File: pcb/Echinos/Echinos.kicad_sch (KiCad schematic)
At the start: 26 parts, among them J1 USB_C_Receptacle_USB2.0, J2 TagConnect_6pins, J3 Pogo, J4 Conn_01x12_Socket, SW1 SW_Push, SW2 SW_Push, U2 W25Q128JVS, U4 USBLC6-2P6, U5 XC6210B332MR-G

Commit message: ✨ ♻️ 🚧 [PCB] - Continue draft schematic with:   - Keyboard matrix + Rotary encoder + analog joystick (specific sheet)   - Rename RP2040 sheet from untitled to RP2040 (make more sense ...)   - MCU first pin assignation
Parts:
- removed C13: 100n, Capacitor_SMD:C_0402_1005Metric, symbol Device:C
- removed C14, C18, C19: 1µ, Capacitor_SMD:C_0603_1608Metric, symbol Device:C
- removed D1: LED, symbol Device:LED
- removed D2: B5817, Diode_SMD:D_SOD-323, symbol Device:D_Schottky
- removed F1: 500mA, Fuse:Fuse_0603_1608Metric, symbol Device:Polyfuse
- removed FB1: FerriteBead_Small, symbol Device:FerriteBead_Small
- removed J1: USB_C_Receptacle_USB2.0, symbol Connector:USB_C_Receptacle_USB2.0
- removed J2: TagConnect_6pins, Connector:Tag-Connect_TC2030-IDC-FP_2x03_P1.27mm_Vertical, symbol Connector:Conn_ARM_SWD_TagConnect_TC2030
- removed J3: Pogo, ptechinos:Pogo_1x04_P2.5mm, symbol Connector_Generic:Conn_01x04
- removed J4: Conn_01x12_Socket, Connector_FFC-FPC:Hirose_FH12-12S-0.5SH_1x12-1MP_P0.50mm_Horizontal, symbol Connector:Conn_01x12_Socket
- removed R10, R11: 4.7kΩ, ptechinos:R_0805_2012Metric, symbol Device:R_Small
- removed R12, R5: 1k, Resistor_SMD:R_0402_1005Metric, symbol Device:R
- removed R2, R3: 5.1k, Resistor_SMD:R_0402_1005Metric, symbol Device:R
- removed R?: 10k, Resistor_SMD:R_0402_1005Metric, symbol Device:R
- removed R?: 27, Resistor_SMD:R_0402_1005Metric, symbol Device:R
- removed SW1, SW2: SW_Push, Button_Switch_SMD:SW_SPST_CK_KXT3, symbol Switch:SW_Push
- removed U2: W25Q128JVS, Package_SO:SOIC-8_5.23x5.23mm_P1.27mm, symbol Memory_Flash:W25Q128JVS
- removed U4: USBLC6-2P6, Package_TO_SOT_SMD:SOT-666, symbol Power_Protection:USBLC6-2P6
- removed U5: XC6210B332MR-G, Package_TO_SOT_SMD:SOT-23-5, symbol Regulator_Linear:XC6210B332MR
- renumbered R6 to R1
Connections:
- net HAND renamed hand
- no-connect marks 4 -> 0
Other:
- removed sheet RP2040
- added sheet Left Side (Left.kicad_sch)
- note removed: "1) Create an all-round contact point between the PCB and the metal housing --> EMI shield 2) Use a ferrite bead to protect against high frequency and force a unique path to ground 3) Avoid any connection (floating) to avoid canceling host shield protection"
- note removed: "??? I2C ???"
- note removed: "Access to Serial Wire Debug multi-drop bus --> Universal tag connector"
- note removed: "Boot / Reset buttons"
- note removed: "Connection between halves"
- note removed: "Debug (Optional)"
- note removed: "ESD protection"
- note removed: "Flash memory"
- note removed: "Max Current Output = 700mA Max Voltage Input = 6V"
- note removed: "On/Off indicator"
- note removed: "Overcurrent protection"
- note removed: "Pull-up resistor used while device is powering up for it to work correctly Resistor must be close to the flash chip"
- note removed: "QSPI lines should be wired as close as possible to MCU to maintain signal integrity"
- note removed: "RP2040"
- note removed: "Resistor must be close to the flash chip Switch pushed (low) --> USB Bootloader Switch released (pulled high) --> Firmware"
- note removed: "Trackball / Trackpad (SPI)"
- note removed: "USB-C connector"
- note removed: "VCC options - 3V and remove R1 to Trackpad PCB - 5V and remove R1/R7/R8 to Trackpad PCB R1 removed --> I2C connection R7/R8 removed --> Support for 5V power"
- note removed: "Voltage clamp"
- note removed: "Voltage regulation"
- moved on the sheet: R1

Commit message: ♻️ [PCB] - Add ferrite bead between shield and ground. Assign hand solder footprints whenever possible. Complete footprint assignation.
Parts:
- R1: footprint Resistor_SMD:R_0402_1005Metric -> Resistor_SMD:R_0402_1005Metric_Pad0.72x0.64mm_HandSolder
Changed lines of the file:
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@@
       (effects (font (size 1.27 1.27)))
     )
-    (property "Footprint" "Resistor_SMD:R_0402_1005Metric" (at 171.45 33.528 90)
+    (property "Footprint" "Resistor_SMD:R_0402_1005Metric_Pad0.72x0.64mm_HandSolder" (at 171.45 33.528 90)
       (effects (font (size 1.27 1.27)) hide)
     )

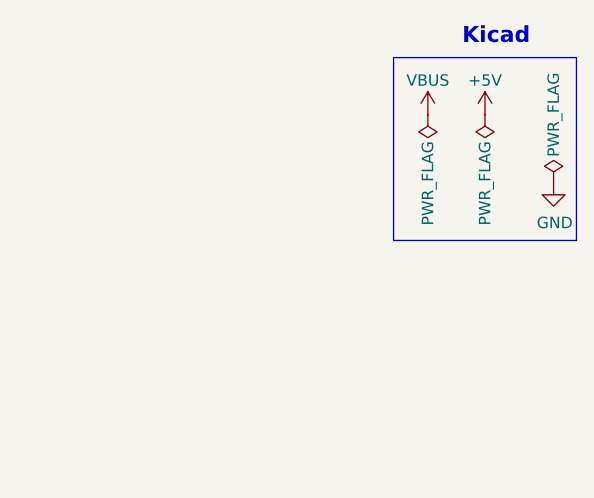
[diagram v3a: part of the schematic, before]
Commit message: ✨ 🐛 ✅ [PCB] - Pass ERC test (exception to unconnected GPIO pins). Fix power symbol assignation to please Kicad. Fix duplicated line name (encoder / joystick) to please Kicad. Add trackball sensor connection documentation. Assign newly created footprints (encoder, joystick, switch).
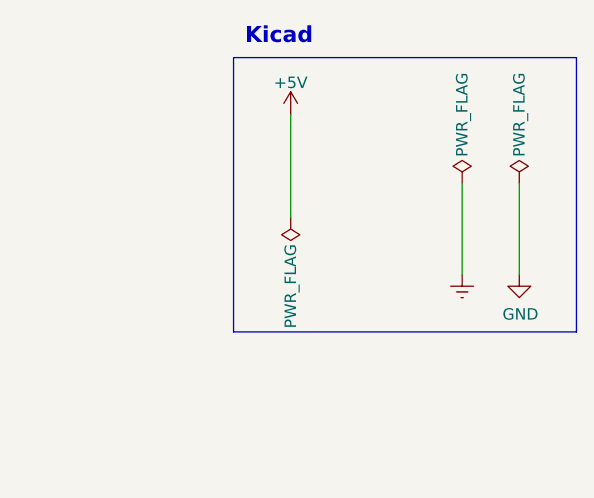
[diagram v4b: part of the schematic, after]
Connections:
- net +3V3 renamed +3.3V
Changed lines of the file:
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@@
     (date "2023-06-10")
   )
+  (wire (pts (xy 273.05 44.45) (xy 273.05 34.29))
+    (stroke (width 0) (type default))
+  )
   (wire (pts (xy 176.53 31.75) (xy 176.53 26.67))
     (stroke (width 0) (type default))
   )
+  (wire (pts (xy 266.7 44.45) (xy 266.7 34.29))
+    (stroke (width 0) (type default))
+  )
   (wire (pts (xy 163.83 31.75) (xy 167.64 31.75))
     (stroke (width 0) (type default))
   )
+  (wire (pts (xy 247.65 26.67) (xy 247.65 38.1))
+    (stroke (width 0) (type default))
+  )
   (wire (pts (xy 175.26 31.75) (xy 176.53 31.75))
     (stroke (width 0) (type default))
@@
     (fill (type none))
   )
-  (rectangle (start 259.08 20.32) (end 279.4 40.64)
+  (rectangle (start 241.3 20.32) (end 279.4 50.8)
     (stroke (width 0) (type default))
     (fill (type none))
@@
     (effects (font (size 1.778 1.778) (thickness 0.3556) bold) (justify left bottom))
   )
-  (text "Kicad" (at 266.7 19.05 0)
+  (text "Kicad" (at 242.57 19.05 0)
     (effects (font (size 1.778 1.778) (thickness 0.3556) bold) (justify left bottom))
   )
@@
     )
   )
-  (symbol (lib_id "power:VBUS") (at 262.89 26.67 0) (unit 1)
-    (in_bom yes) (on_board yes) (dnp no)
-    (property "Reference" "#PWR02" (at 262.89 30.48 0)
-      (effects (font (size 1.27 1.27)) hide)
-    )
-    (property "Value" "VBUS" (at 262.89 22.86 0)
-      (effects (font (size 1.27 1.27)))
-    )
-    (property "Footprint" "" (at 262.89 26.67 0)
-      (effects (font (size 1.27 1.27)) hide)
-    )
-    (property "Datasheet" "" (at 262.89 26.67 0)
+  (symbol (lib_id "power:+5V") (at 247.65 26.67 0) (unit 1)
+    (in_bom yes) (on_board yes) (dnp no)
+    (property "Reference" "#PWR02" (at 247.65 30.48 0)
+      (effects (font (size 1.27 1.27)) hide)
+    )
+    (property "Value" "+5V" (at 247.65 23.114 0)
+      (effects (font (size 1.27 1.27)))
+    )
+    (property "Footprint" "" (at 247.65 26.67 0)
+      (effects (font (size 1.27 1.27)) hide)
+    )
+    (property "Datasheet" "" (at 247.65 26.67 0)
       (effects (font (size 1.27 1.27)) hide)
     )
@@
     )
   )
-  (symbol (lib_id "power:GND") (at 276.86 34.29 0) (unit 1)
-    (in_bom yes) (on_board yes) (dnp no)
-    (property "Reference" "#PWR04" (at 276.86 40.64 0)
-      (effects (font (size 1.27 1.27)) hide)
-    )
-    (property "Value" "GND" (at 276.987 38.6842 0)
-      (effects (font (size 1.27 1.27)))
-    )
-    (property "Footprint" "" (at 276.86 34.29 0)
-      (effects (font (size 1.27 1.27)) hide)
-    )
-    (property "Datasheet" "" (at 276.86 34.29 0)
-      (effects (font (size 1.27 1.27)) hide)
-    )
-    (pin "1")
-    (instances
-      (project "Echinos"
-        (path "/5bd3006d-ec09-4ffb-bec3-03fa5613b46a"
-          (reference "#PWR04") (unit 1)
+  (symbol (lib_id "power:PWR_FLAG") (at 266.7 34.29 0) (unit 1)
+    (in_bom yes) (on_board yes) (dnp no)
+    (property "Reference" "#FLG03" (at 266.7 32.385 0)
+      (effects (font (size 1.27 1.27)) hide)
+    )
+    (property "Value" "PWR_FLAG" (at 266.7 26.67 90)
+      (effects (font (size 1.27 1.27)))
+    )
+    (property "Footprint" "" (at 266.7 34.29 0)
+      (effects (font (size 1.27 1.27)) hide)
+    )
+    (property "Datasheet" "~" (at 266.7 34.29 0)
+      (effects (font (size 1.27 1.27)) hide)
+    )
+    (pin "1")
+    (instances
+      (project "Echinos"
+        (path "/5bd3006d-ec09-4ffb-bec3-03fa5613b46a"
+          (reference "#FLG03") (unit 1)
+        )
+      )
+    )
+  )
+  (symbol (lib_id "power:GND") (at 273.05 44.45 0) (unit 1)
+    (in_bom yes) (on_board yes) (dnp no)
+    (property "Reference" "#PWR03" (at 273.05 50.8 0)
+      (effects (font (size 1.27 1.27)) hide)
+    )
+    (property "Value" "GND" (at 273.177 48.8442 0)
+      (effects (font (size 1.27 1.27)))
+    )
+    (property "Footprint" "" (at 273.05 44.45 0)
+      (effects (font (size 1.27 1.27)) hide)
+    )
+    (property "Datasheet" "" (at 273.05 44.45 0)
+      (effects (font (size 1.27 1.27)) hide)
+    )
+    (pin "1")
+    (instances
+      (project "Echinos"
+        (path "/5bd3006d-ec09-4ffb-bec3-03fa5613b46a"
+          (reference "#PWR03") (unit 1)
         )
       )
@@
     )
   )
-  (symbol (lib_id "power:PWR_FLAG") (at 276.86 34.29 0) (unit 1)
-    (in_bom yes) (on_board yes) (dnp no)
-    (property "Reference" "#FLG03" (at 276.86 32.385 0)
-      (effects (font (size 1.27 1.27)) hide)
-    )
-    (property "Value" "PWR_FLAG" (at 276.86 26.67 90)
-      (effects (font (size 1.27 1.27)))
-    )
-    (property "Footprint" "" (at 276.86 34.29 0)
-      (effects (font (size 1.27 1.27)) hide)
-    )
-    (property "Datasheet" "~" (at 276.86 34.29 0)
-      (effects (font (size 1.27 1.27)) hide)
-    )
-    (pin "1")
-    (instances
-      (project "Echinos"
-        (path "/5bd3006d-ec09-4ffb-bec3-03fa5613b46a"
-          (reference "#FLG03") (unit 1)
-        )
-      )
-    )
-  )
-  (symbol (lib_id "power:PWR_FLAG") (at 262.89 26.67 180) (unit 1)
-    (in_bom yes) (on_board yes) (dnp no)
-    (property "Reference" "#FLG01" (at 262.89 28.575 0)
-      (effects (font (size 1.27 1.27)) hide)
-    )
-    (property "Value" "PWR_FLAG" (at 262.89 34.29 90)
-      (effects (font (size 1.27 1.27)))
-    )
-    (property "Footprint" "" (at 262.89 26.67 0)
-      (effects (font (size 1.27 1.27)) hide)
-    )
-    (property "Datasheet" "~" (at 262.89 26.67 0)
+  (symbol (lib_id "power:PWR_FLAG") (at 247.65 38.1 180) (unit 1)
+    (in_bom yes) (on_board yes) (dnp no)
+    (property "Reference" "#FLG01" (at 247.65 40.005 0)
+      (effects (font (size 1.27 1.27)) hide)
+    )
+    (property "Value" "PWR_FLAG" (at 247.65 45.72 90)
+      (effects (font (size 1.27 1.27)))
+    )
+    (property "Footprint" "" (at 247.65 38.1 0)
+      (effects (font (size 1.27 1.27)) hide)
+    )
+    (property "Datasheet" "~" (at 247.65 38.1 0)
       (effects (font (size 1.27 1.27)) hide)
     )
@@
     )
   )
-  (symbol (lib_id "power:PWR_FLAG") (at 269.24 26.67 180) (unit 1)
-    (in_bom yes) (on_board yes) (dnp no)
-    (property "Reference" "#FLG02" (at 269.24 28.575 0)
-      (effects (font (size 1.27 1.27)) hide)
-    )
-    (property "Value" "PWR_FLAG" (at 269.24 34.29 90)
-      (effects (font (size 1.27 1.27)))
-    )
-    (property "Footprint" "" (at 269.24 26.67 0)
-      (effects (font (size 1.27 1.27)) hide)
-    )
-    (property "Datasheet" "~" (at 269.24 26.67 0)
+  (symbol (lib_id "power:PWR_FLAG") (at 273.05 34.29 0) (unit 1)
+    (in_bom yes) (on_board yes) (dnp no)
+    (property "Reference" "#FLG02" (at 273.05 32.385 0)
+      (effects (font (size 1.27 1.27)) hide)
+    )
+    (property "Value" "PWR_FLAG" (at 273.05 26.67 90)
+      (effects (font (size 1.27 1.27)))
+    )
+    (property "Footprint" "" (at 273.05 34.29 0)
+      (effects (font (size 1.27 1.27)) hide)
+    )
+    (property "Datasheet" "~" (at 273.05 34.29 0)
       (effects (font (size 1.27 1.27)) hide)
     )
@@
     )
   )
-  (symbol (lib_id "power:+5V") (at 269.24 26.67 0) (unit 1)
-    (in_bom yes) (on_board yes) (dnp no)
-    (property "Reference" "#PWR03" (at 269.24 30.48 0)
-      (effects (font (size 1.27 1.27)) hide)
-    )
-    (property "Value" "+5V" (at 269.24 22.86 0)
-      (effects (font (size 1.27 1.27)))
-    )
-    (property "Footprint" "" (at 269.24 26.67 0)
-      (effects (font (size 1.27 1.27)) hide)
-    )
-    (property "Datasheet" "" (at 269.24 26.67 0)
-      (effects (font (size 1.27 1.27)) hide)
-    )
-    (pin "1")
-    (instances
-      (project "Echinos"
-        (path "/5bd3006d-ec09-4ffb-bec3-03fa5613b46a"
-          (reference "#PWR03") (unit 1)
-        )
-      )
+  (symbol (lib_id "power:Earth") (at 266.7 44.45 0) (unit 1)
+    (in_bom yes) (on_board yes) (dnp no) (fields_autoplaced)
+    (property "Reference" "#PWR014" (at 266.7 50.8 0)
+      (effects (font (size 1.27 1.27)) hide)
+    )
+    (property "Value" "Earth" (at 266.7 48.26 0)
+      (effects (font (size 1.27 1.27)) hide)
+    )
+    (property "Footprint" "" (at 266.7 44.45 0)
+      (effects (font (size 1.27 1.27)) hide)
+    )
+    (property "Datasheet" "~" (at 266.7 44.45 0)
+      (effects (font (size 1.27 1.27)) hide)
+    )
+    (pin "1")
+    (instances
+      (project "Echinos"
+        (path "/5bd3006d-ec09-4ffb-bec3-03fa5613b46a/82089e05-aeac-4bc0-b466-29ce28ef1ab1"
+          (reference "#PWR014") (unit 1)
+        )
+        (path "/5bd3006d-ec09-4ffb-bec3-03fa5613b46a"
+          (reference "#PWR051") (unit 1)
+        )
+      )

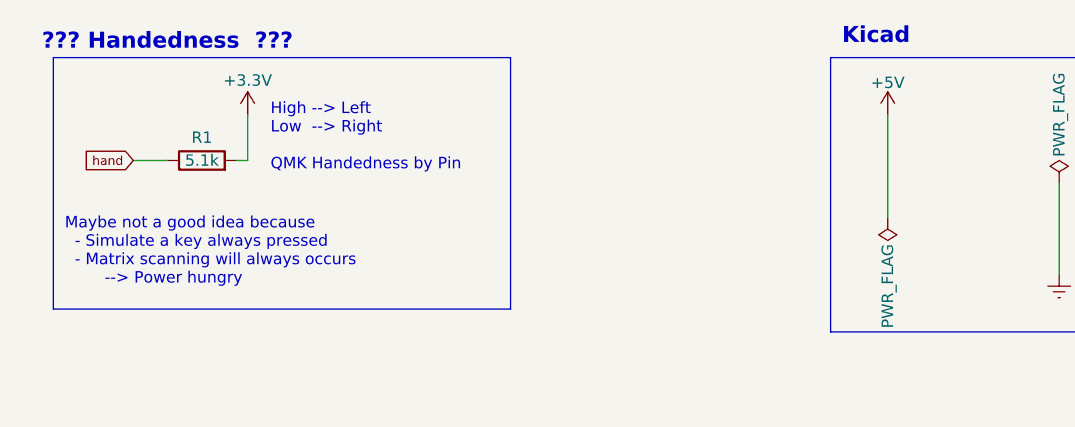
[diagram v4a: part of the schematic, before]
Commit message: ✨ [PCB] - Complete schema and PCB for left halve. All connections are made. Optional encoder on the top outer key Optional joystick on either outer thumb or above middle thumb. Optional power LED (jumpers) SATA to connect both sides VIK compatible (except for 5.0V track) with enough space on the inner side to clip a VIK module Remaining MCU pins exposed with a 2.54mm spaced header All VIK modules are not yet placed / routed.
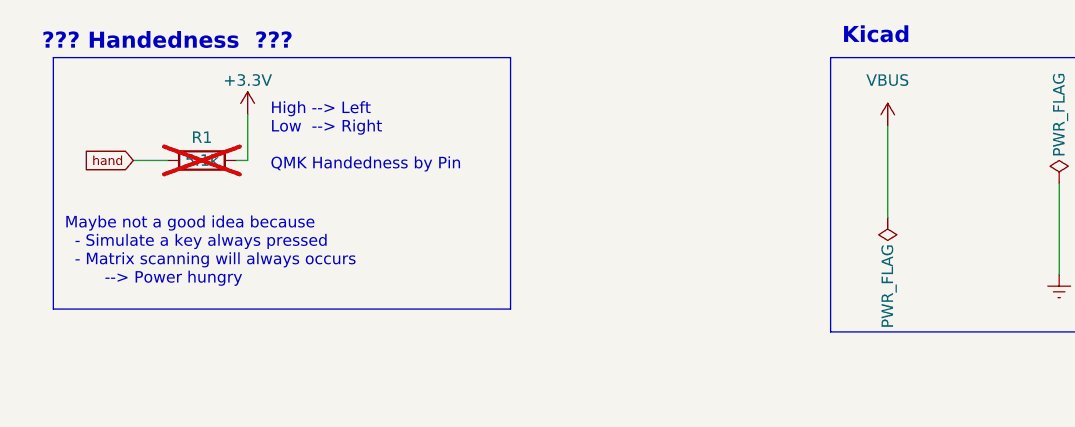
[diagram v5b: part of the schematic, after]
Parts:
- R1: now not fitted; now left out of the parts list

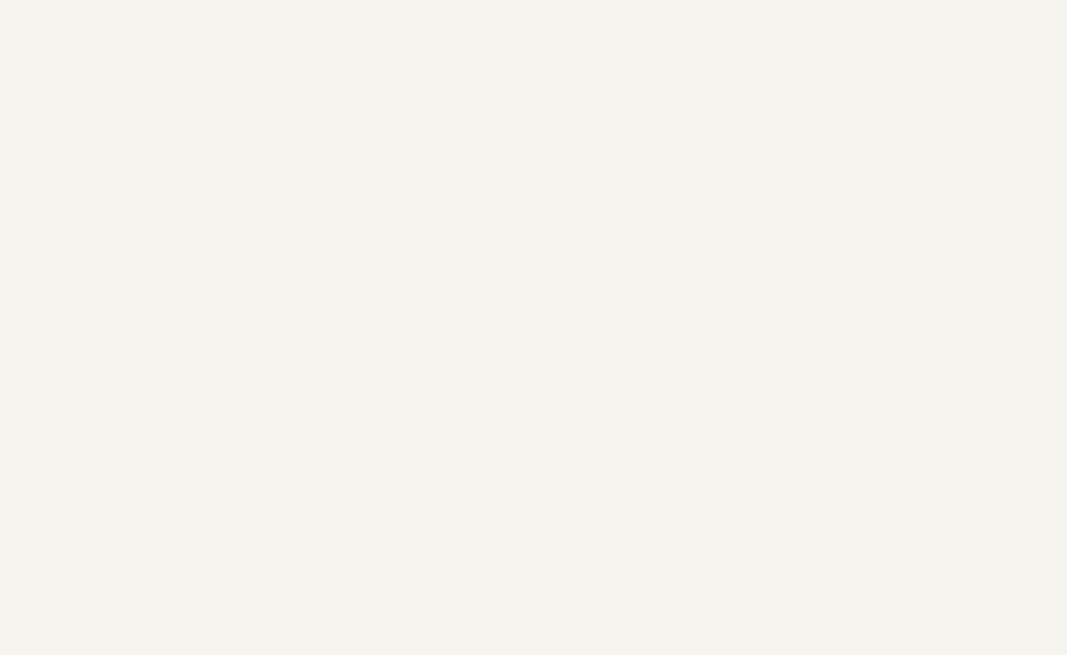
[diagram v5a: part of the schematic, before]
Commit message: 🚧 [PCB] - Backup of a specific layout around MCU. Modules moved to a specific schematic page.
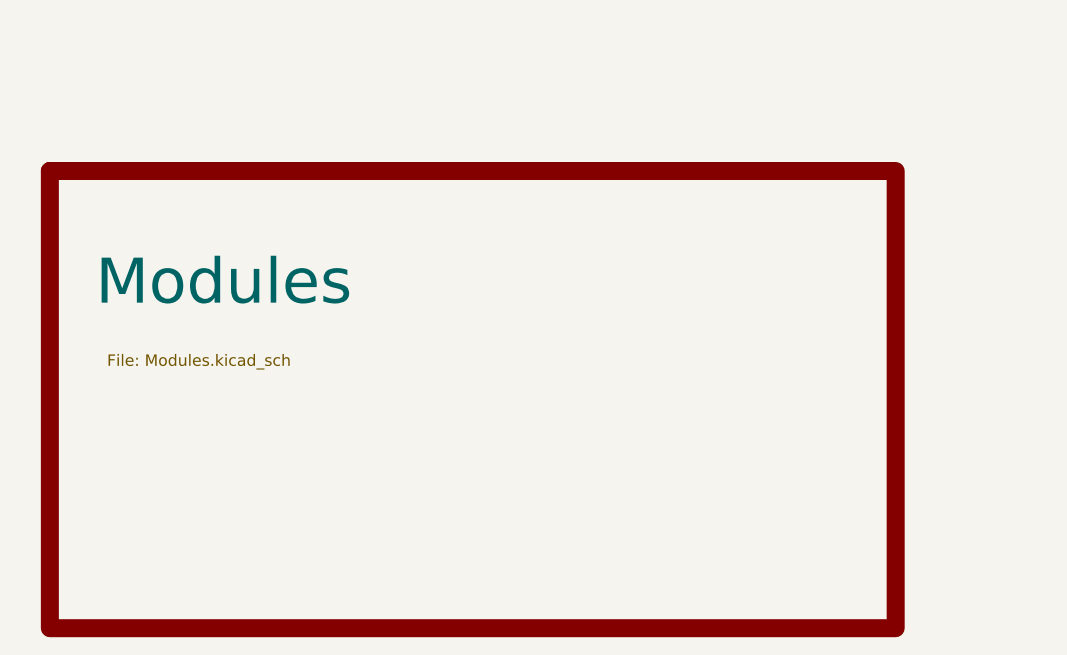
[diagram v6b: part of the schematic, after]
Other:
- added sheet Modules (Modules.kicad_sch)
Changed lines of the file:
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@@
+    )
+  )
+  (sheet (at 20.32 140.97) (size 93.98 50.8)
+    (stroke (width 2) (type solid) (color 0 132 132 1))
+    (fill (color 0 0 0 0.0000))
+    (property "Sheetname" "Modules" (at 25.4 156.21 0)
+      (effects (font (size 5 5)) (justify left bottom))
+    )
+    (property "Sheetfile" "Modules.kicad_sch" (at 26.67 161.29 0)
+      (effects (font (size 1.27 1.27)) (justify left top))
+    )
+    (instances
+      (project "Echinos"
+        (path "/5bd3006d-ec09-4ffb-bec3-03fa5613b46a/82089e05-aeac-4bc0-b466-29ce28ef1ab1" (page "6"))
+        (path "/5bd3006d-ec09-4ffb-bec3-03fa5613b46a" (page "6"))
+      )
     )
   )
